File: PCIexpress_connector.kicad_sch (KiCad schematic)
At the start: 2 parts, among them J1 PCIexpress_bracket, J2 PCIexpress_x4

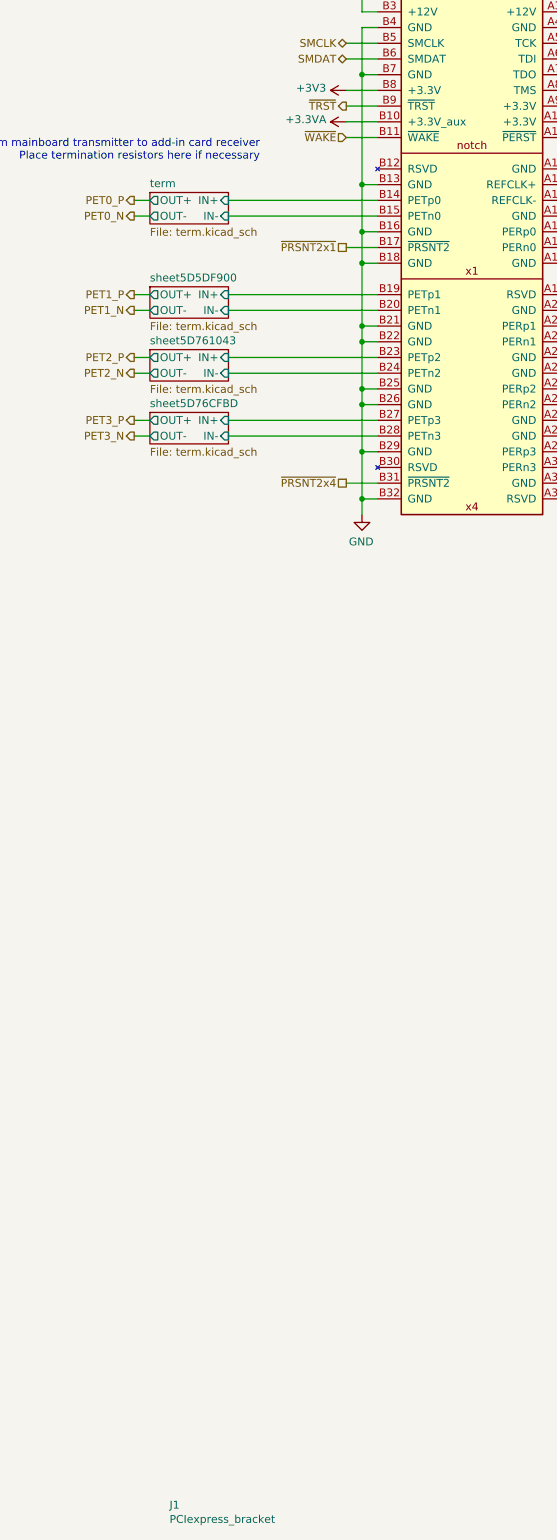
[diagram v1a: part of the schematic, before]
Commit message: updated schematic working on layout
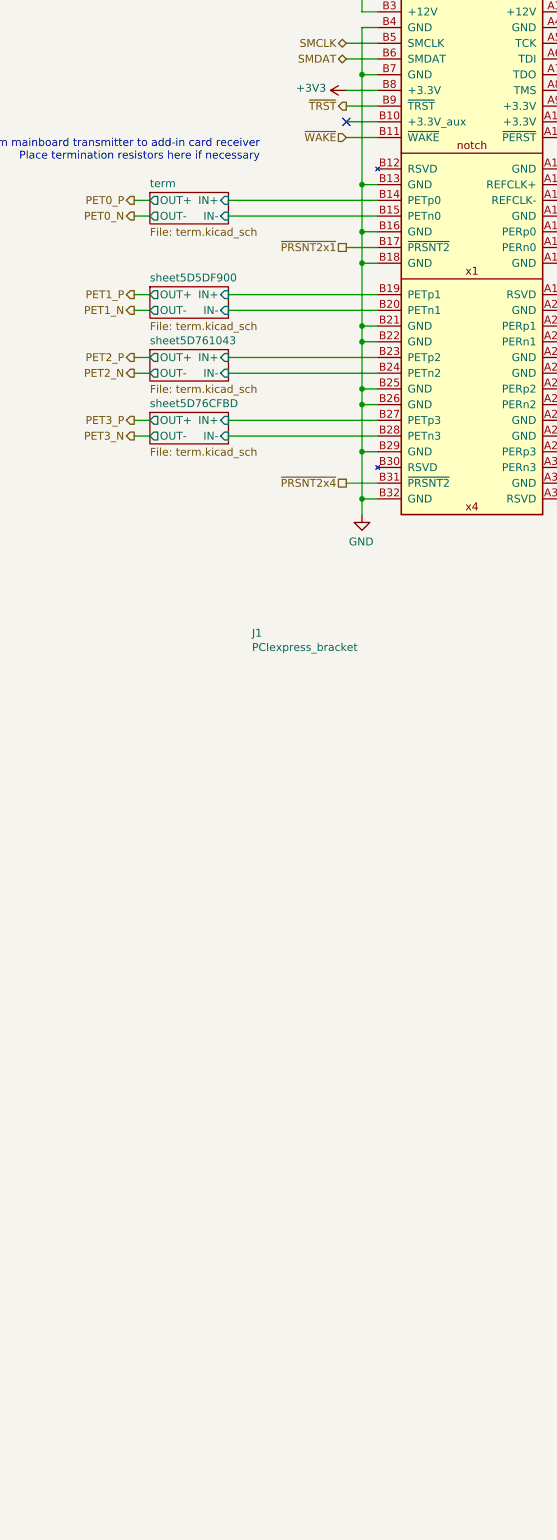
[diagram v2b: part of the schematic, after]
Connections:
- net +3.3VA: no longer names the net of J2.B10 (+3.3V_aux)
- no-connect marks 0 -> 1
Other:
- company: Author: Luca Anastasio -> Author: Aadhi M
- title: PCIexpress_x4_full -> PC-AXE
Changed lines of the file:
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@@
 	(paper "A4" portrait)
 	(title_block
-		(title "PCIexpress_x4_full")
-		(company "Author: Luca Anastasio")
+		(title "PC-AXE")
+		(company "Author: Aadhi M")
 	)
 	(text "From mainboard transmitter to add-in card receiver\nPlace termination resistors here if necessary"
@@
 		(diameter 0)
 		(color 0 0 0 0)
+	)
+	(no_connect
+		(at 85.09 48.26)
 	)
 	(wire
@@
 	(symbol
 		(lib_id "PCIexpress:PCIexpress_bracket")
-		(at 55.88 273.05 0)
+		(at 69.215 132.08 0)
 		(unit 1)
 		(exclude_from_sim no)
@@
 		(dnp no)
 		(property "Reference" "J1"
-			(at 56.515 271.8816 0)
+			(at 69.85 130.9116 0)
 			(effects
 				(font
@@
 		)
 		(property "Value" "PCIexpress_bracket"
-			(at 56.515 274.193 0)
+			(at 69.85 133.223 0)
 			(effects
 				(font
@@
 		)
 		(property "Footprint" "PCIexpress:PCIexpress_bracket_full"
-			(at 55.88 273.05 0)
+			(at 69.215 132.08 0)
 			(effects
 				(font
@@
 		)
 		(property "Datasheet" ""
-			(at 55.88 273.05 0)
+			(at 69.215 132.08 0)
 			(effects
 				(font
@@
 		)
 		(property "Description" ""
-			(at 55.88 273.05 0)
+			(at 69.215 132.08 0)
 			(effects
 				(font
@@
 					(unit 1)
 				)
-			)
-		)
-	)
-	(symbol
-		(lib_id "power:+3.3VA")
-		(at 85.09 48.26 90)
-		(unit 1)
-		(exclude_from_sim no)
-		(in_bom yes)
-		(on_board yes)
-		(dnp no)
-		(property "Reference" "#PWR02"
-			(at 88.9 48.26 0)
-			(effects
-				(font
-					(size 1.27 1.27)
-				)
-				(hide yes)
-			)
-		)
-		(property "Value" "+3.3VA"
-			(at 81.8642 47.879 90)
-			(effects
-				(font
-					(size 1.27 1.27)
-				)
-				(justify left)
-			)
-		)
-		(property "Footprint" ""
-			(at 85.09 48.26 0)
-			(effects
-				(font
-					(size 1.27 1.27)
-				)
-				(hide yes)
-			)
-		)
-		(property "Datasheet" ""
-			(at 85.09 48.26 0)
-			(effects
-				(font
-					(size 1.27 1.27)
-				)
-				(hide yes)
-			)
-		)
-		(property "Description" ""
-			(at 85.09 48.26 0)
-			(effects
-				(font
-					(size 1.27 1.27)
-				)
-				(hide yes)
-			)
-		)
-		(pin "1"
-		)
-		(instances
-			(project ""
-				(path "/540dc3bd-590a-41f0-90cd-0aeeeb4ef5ba/00000000-0000-0000-0000-00005d508b15"
-					(reference "#PWR02")
-					(unit 1)
-				)
